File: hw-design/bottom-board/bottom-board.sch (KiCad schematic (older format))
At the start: 0 parts

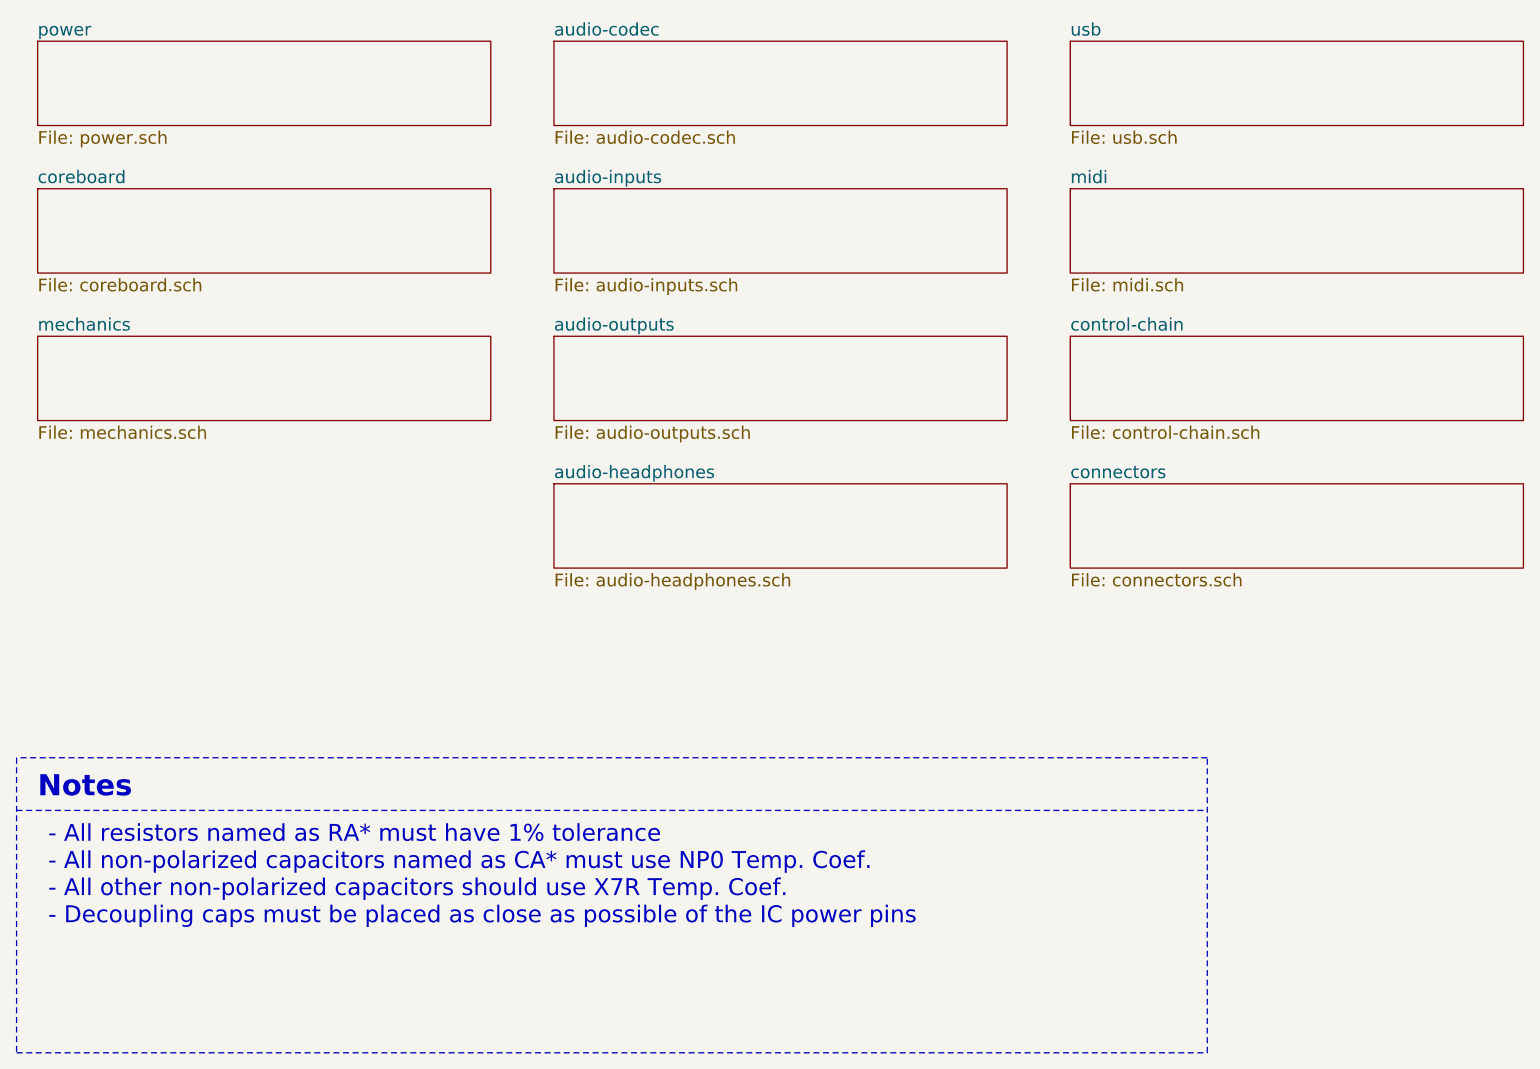
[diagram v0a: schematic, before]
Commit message: changed a bottomboard to a minimal HMI testing unit
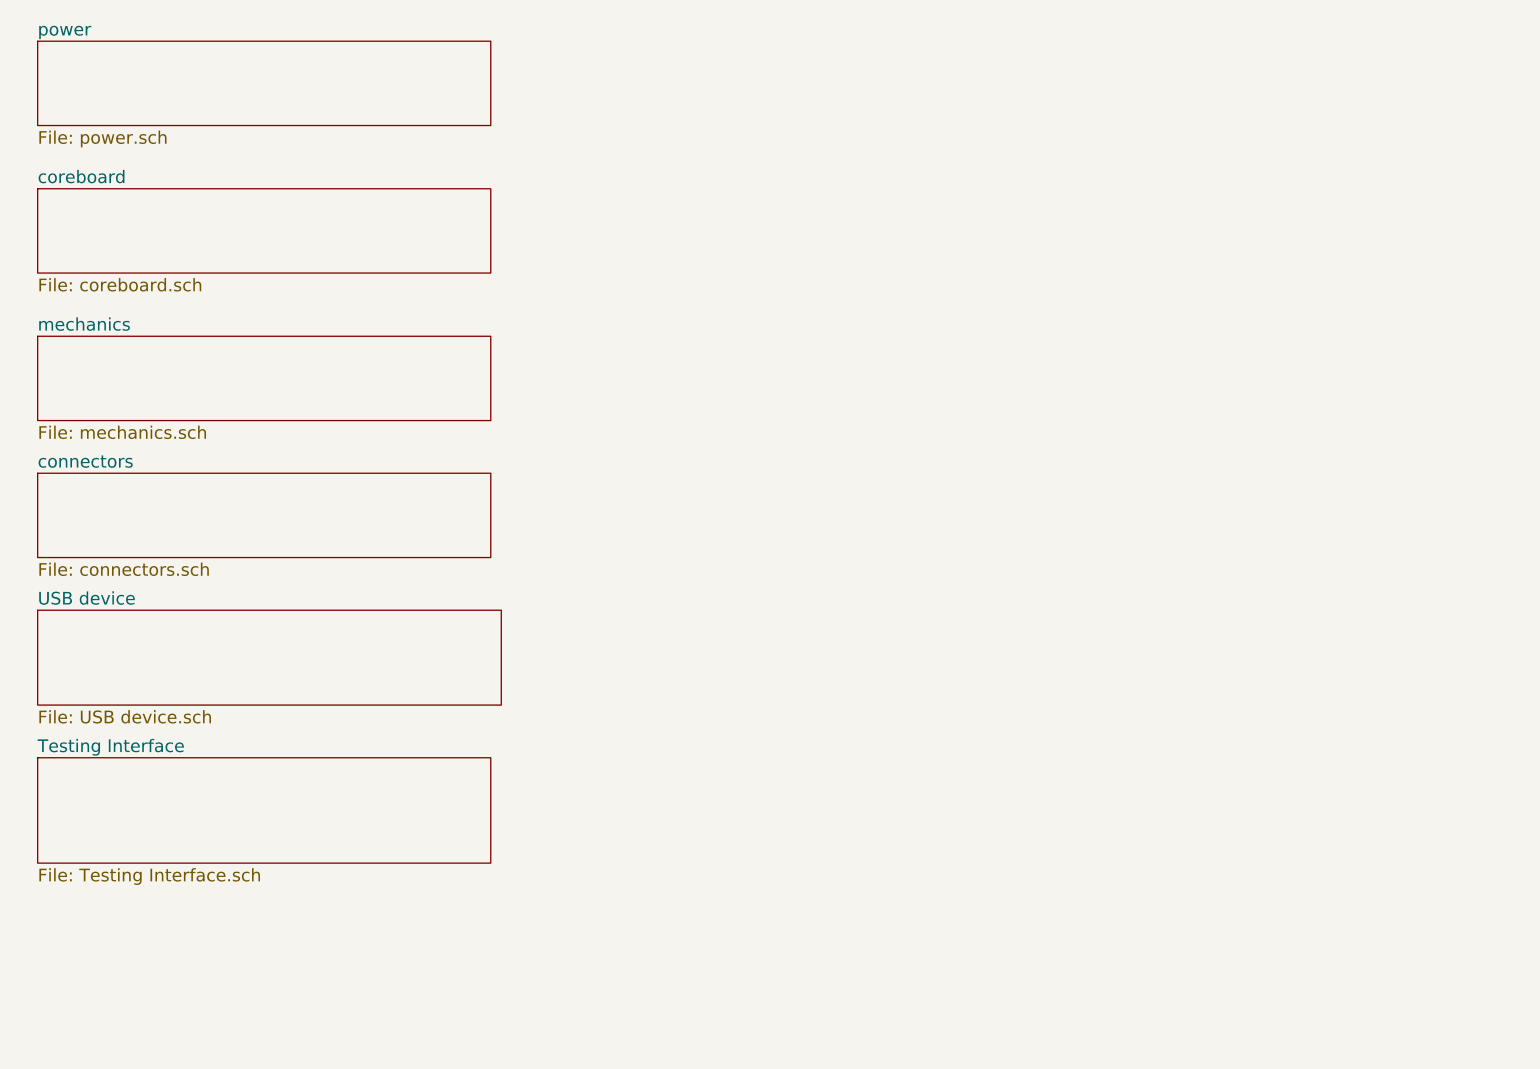
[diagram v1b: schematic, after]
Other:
- note removed: "- All resistors named as RA* must have 1% tolerance\n- All non-polarized capacitors named as CA* must use NP0 Temp. Coef.\n- All other non-polarized capacitors should use X7R Temp. Coef.\n- Decoupling caps must be placed as close as possible of the IC power pins"
- note removed: "Notes\n"
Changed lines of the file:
@@
 EESchema Schematic File Version 4
 LIBS:bottom-board-cache
-EELAYER 26 0
+EELAYER 29 0
 EELAYER END
 $Descr A4 11693 8268
 encoding utf-8
-Sheet 1 12
-Title "MOD Duo - Bottom Board"
+Sheet 1 7
+Title "MOD Duo -HMI testing board"
 Date ""
-Rev ""
-Comp "MOD"
-Comment1 ""
-Comment2 ""
-Comment3 ""
-Comment4 ""
+Rev "1.0"
+Comp "MOD Devices GmbH"
+Comment1 "Controller board Tester"
+Comment2 "used for the MOD Duo"
+Comment3 "or MOD Duo X controller"
+Comment4 "Compatible w/ Marsboard SoM"
 $EndDescr
 $Sheet
@@
 $EndSheet
 $Sheet
-S 3750 850  2150 400
-U 54F72B97
-F0 "audio-codec" 60
-F1 "audio-codec.sch" 60
-$EndSheet
-$Sheet
 S 1300 1550 2150 400
 U 54F725AE
@@
 $EndSheet
 $Sheet
-S 3750 1550 2150 400
-U 54F72C8D
-F0 "audio-inputs" 60
-F1 "audio-inputs.sch" 60
-$EndSheet
-$Sheet
-S 3750 2250 2150 400
-U 54F72CD0
-F0 "audio-outputs" 60
-F1 "audio-outputs.sch" 60
-$EndSheet
-$Sheet
-S 3750 2950 2150 400
-U 54F72F64
-F0 "audio-headphones" 60
-F1 "audio-headphones.sch" 60
-$EndSheet
-$Sheet
-S 6200 850  2150 400
-U 54F72FB2
-F0 "usb" 60
-F1 "usb.sch" 60
-$EndSheet
-$Sheet
-S 6200 1550 2150 400
-U 54F72FB4
-F0 "midi" 60
-F1 "midi.sch" 60
-$EndSheet
-$Sheet
-S 6200 2250 2150 400
-U 54F72FB6
-F0 "control-chain" 60
-F1 "control-chain.sch" 60
-$EndSheet
-$Sheet
-S 6200 2950 2150 400
+S 1300 2900 2150 400
 U 54F72FB8
 F0 "connectors" 60
 F1 "connectors.sch" 60
 $EndSheet
-Text Notes 1350 5050 0    80   ~ 0
-- All resistors named as RA* must have 1% tolerance\n- All non-polarized capacitors named as CA* must use NP0 Temp. Coef.\n- All other non-polarized capacitors should use X7R Temp. Coef.\n- Decoupling caps must be placed as close as possible of the IC power pins
-Text Notes 1300 4450 0    100  ~ 20
-Notes\n
-Wire Notes Line
-	1200 5650 6850 5650
-Wire Notes Line
-	6850 5650 6850 4250
-Wire Notes Line
-	6850 4250 1200 4250
-Wire Notes Line
-	1200 4500 6850 4500
 $Sheet
 S 1300 2250 2150 400
@@
 F1 "mechanics.sch" 60
 $EndSheet
-Wire Notes Line
-	1200 4250 1200 5650
+$Sheet
+S 1300 3550 2200 450
+U 5CFC887F
+F0 "USB device" 60
+F1 "USB device.sch" 60
+$EndSheet
+$Sheet
+S 1300 4250 2150 500
+U 5CFD694C
+F0 "Testing Interface" 60
+F1 "Testing Interface.sch" 60
+$EndSheet
 $EndSCHEMATC
